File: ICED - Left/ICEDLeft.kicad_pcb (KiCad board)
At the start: 2 copper layers, 175.4 x 145 mm, 150 parts, among them P1 Conn_ARM_JTAG_SWD_10, P2 USBC, P3 CONN_17, P4 USB3_AFEMALE, P5 RGB Out, Q1 TC1264, U1 MK20DX256VLH7, U2 IS31FL3737-QFLS4-TR, X1 CRYSTAL

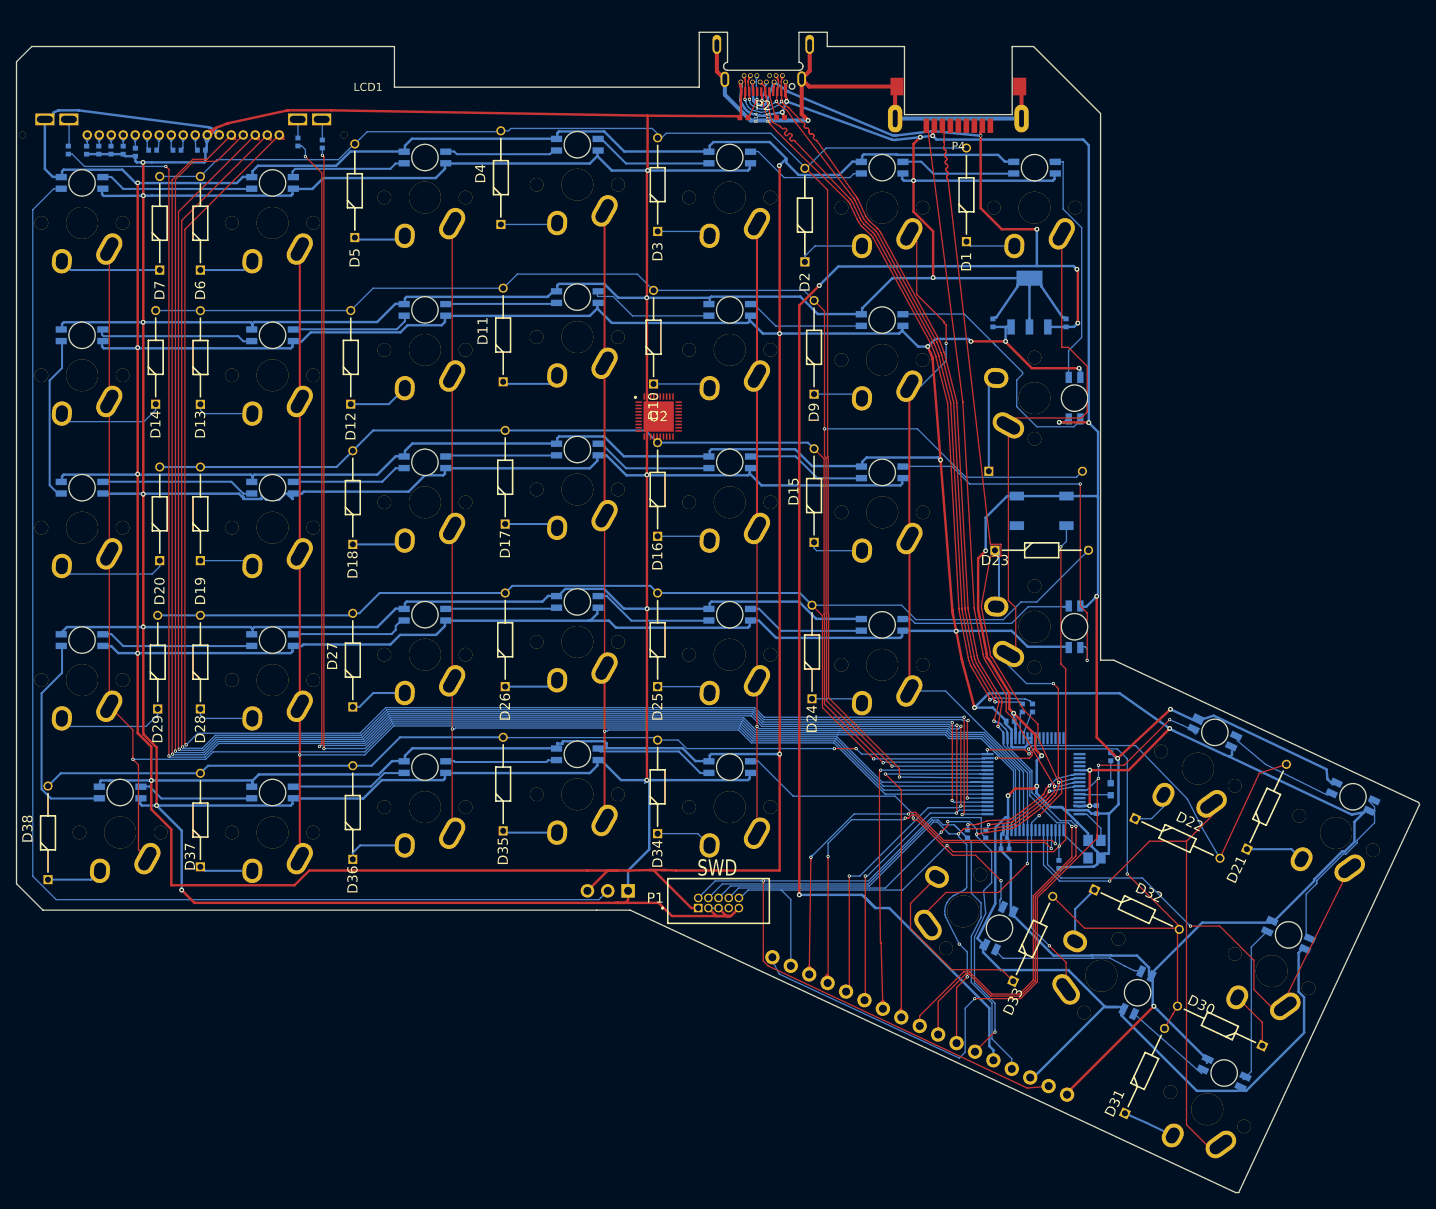
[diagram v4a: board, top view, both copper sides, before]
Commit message: Added support caps
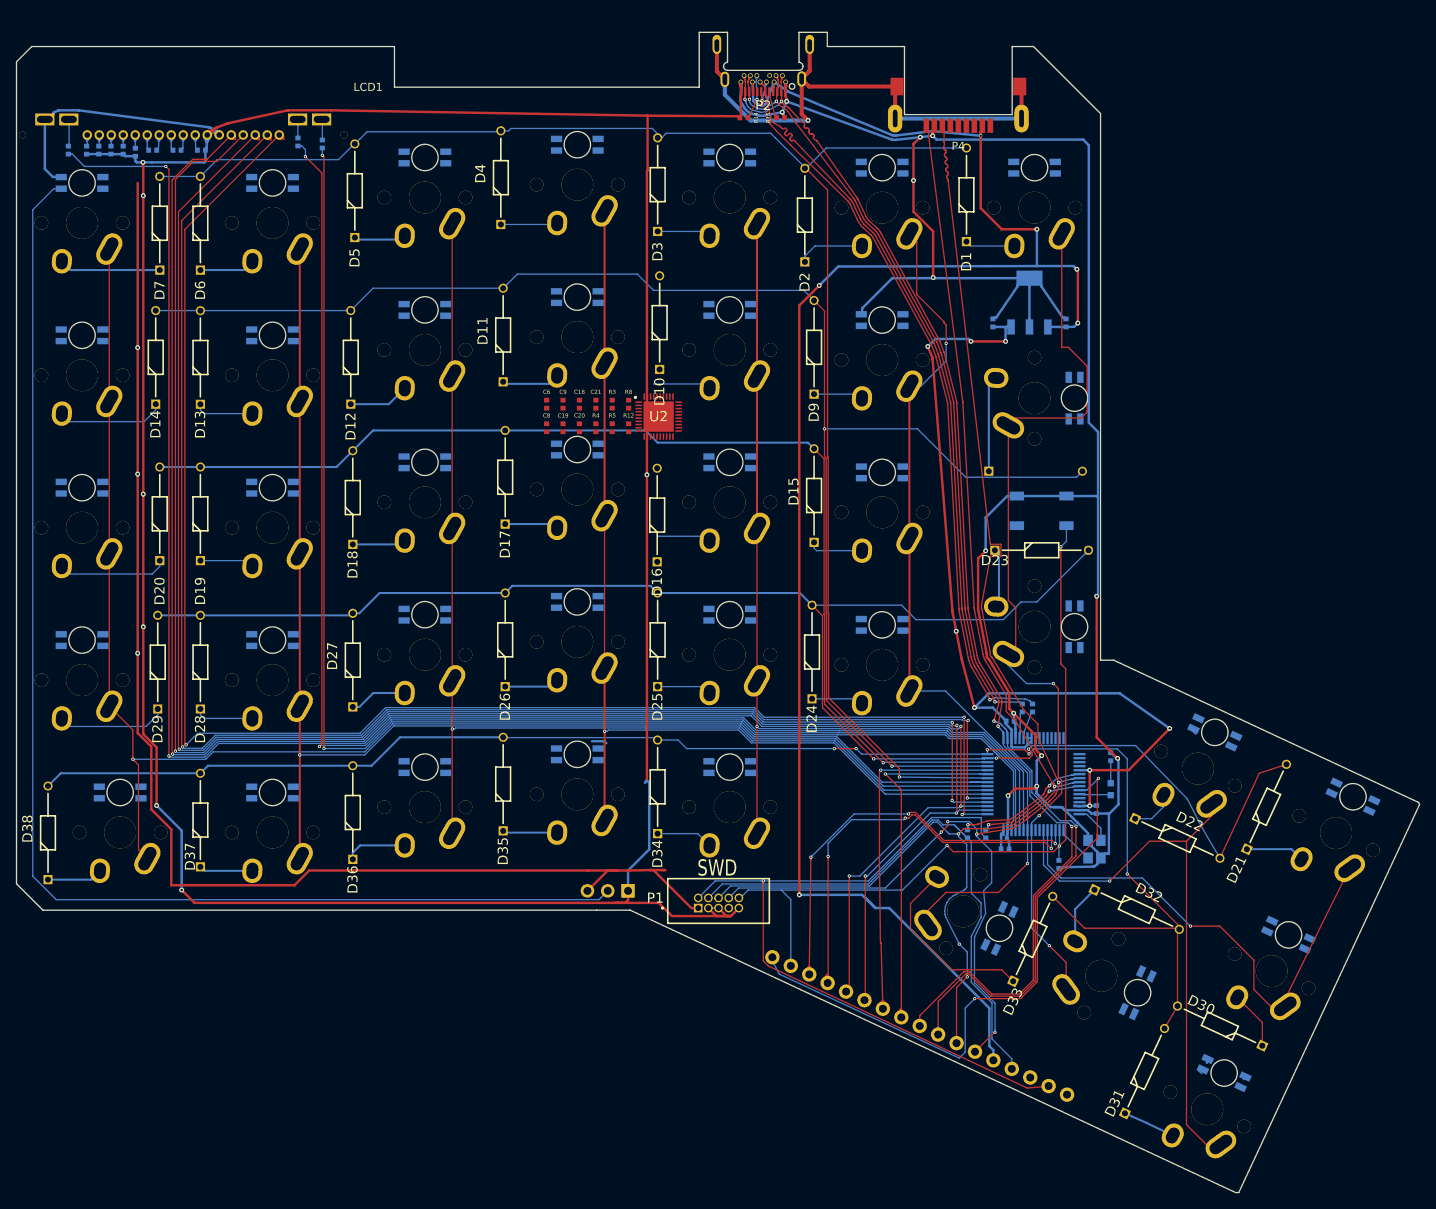
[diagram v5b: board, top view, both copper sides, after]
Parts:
- added C18: 0.1uF, prettylib:SMD-1005, F.Cu at (88.0, 72.3)
- added C19: 0.1uF, prettylib:SMD-1005, F.Cu at (86.0, 75.2)
- added C20: 0.1uF, prettylib:SMD-1005, F.Cu at (88.0, 75.2)
- added C21: 0.47uF, prettylib:SMD-1005, F.Cu at (90.1, 72.3)
- added C6: 0.47uF, prettylib:SMD-1005, F.Cu at (83.9, 72.3)
- added C8: 0.47uF, prettylib:SMD-1005, F.Cu at (83.9, 75.2)
- added C9: 0.47uF, prettylib:SMD-1005, F.Cu at (86.0, 72.3)
- added R12: 20k, prettylib:SMD-1005, F.Cu at (94.2, 75.2)
- added R3: 4.7, prettylib:SMD-1005, F.Cu at (92.1, 72.3)
- added R4: 100k, prettylib:SMD-1005, F.Cu at (90.1, 75.2)
- added R5: 4.7, prettylib:SMD-1005, F.Cu at (92.1, 75.2)
- added R8: 100k, prettylib:SMD-1005, F.Cu at (94.2, 72.3)
- moved D16 3.20 mm to (97.7, 92.0)
- moved D10 1.97 mm to (98.0, 67.9)
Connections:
- U1 pad 39: (no net) -> /mcu/SDB
- U1 pad 40: (no net) -> /Col7
- U1 pad 55: /Col7 -> (no net)
- U1 pad 56: /Col8 -> (no net)
- U2 pad 19: (no net) -> VDD
- U2 pad 26: (no net) -> VDD
- U2 pad 29: (no net) -> /mcu/ledmatrix_2/GND
- U2 pad 31: (no net) -> VDD
- U2 pad 34: (no net) -> /mcu/SDA0
- U2 pad 35: (no net) -> /mcu/SCL0
- U2 pad 36: (no net) -> /mcu/ledmatrix_2/GND
- U2 pad 38: (no net) -> /mcu/SDB
- U2 pad 39: (no net) -> /mcu/ledmatrix_2/IICRST
- U2 pad 4: (no net) -> /mcu/ledmatrix_2/GND
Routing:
- net VDD: track 1142.2 -> 320.8 mm, vias 19 -> 11
- net VSS: track 1298.4 -> 672.9 mm, vias 28 -> 20
- net /ledmatrix/RGBIN: track 92.8 -> 0.00 mm, vias 4 -> 0
- net /mcu/RGBIN: track 0.00 -> 76.1 mm, vias 0 -> 2
- net /mcu/ledmatrix_2/Green3: track 66.0 -> 0.00 mm
- net /mcu/ledmatrix_2/Row1A: track 49.1 -> 0.00 mm
- net /mcu/ledmatrix_2/Row3A: track 48.9 -> 0.00 mm
- net /mcu/ledmatrix_2/Row4B: track 48.1 -> 0.00 mm, vias 2 -> 0
- net /mcu/ledmatrix_2/Green1: track 47.4 -> 0.96 mm
- net /mcu/ledmatrix_2/Row5A: track 44.2 -> 0.00 mm
- net /mcu/ledmatrix_2/Row5B: track 41.5 -> 0.69 mm, vias 2 -> 0
- net Net-(LED8-Pad4): track 32.4 -> 0.00 mm
- net /mcu/ledmatrix_2/Row1B: track 30.3 -> 0.37 mm
- net /mcu/ledmatrix_2/Row2B: track 29.8 -> 0.00 mm
- net Net-(LED23-Pad4): track 22.6 -> 0.00 mm
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
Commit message: left 50% routed
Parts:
- moved R4 25.4 mm to (107.7, 93.5)
- moved R3 24.9 mm to (104.4, 94.0)
- moved R8 23.5 mm to (103.0, 94.1)
- moved R5 23.4 mm to (106.1, 94.0)
- moved C8 18.6 mm to (102.5, 74.2), turned to 180 degrees
- moved C19 17.9 mm to (103.8, 74.2), turned to 180 degrees
- moved C6 16.6 mm to (99.2, 78.9), turned to 180 degrees
- moved C9 15.5 mm to (101.1, 69.0)
- moved C18 13.9 mm to (100.3, 78.9), turned to 180 degrees
- moved C20 13.4 mm to (99.9, 69.0)
- moved C21 9.05 mm to (98.5, 69.0)
- moved R12 8.67 mm to (102.3, 72.3), turned to 90 degrees
- moved D10 1.17 mm to (96.9, 67.7)
- moved D26 0.90 mm to (78.6, 106.7)
- moved D36 0.63 mm to (59.2, 128.8)
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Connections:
- R12 pad 1: VSS -> /mcu/ledmatrix_2/RSET
- R12 pad 2: (no net) -> VSS
- U2 pad 30: (no net) -> /mcu/ledmatrix_2/RSET
- U2 pad 32: (no net) -> VDD
- U2 pad 6: /mcu/ledmatrix_2/Blue2 -> /mcu/ledmatrix_2/Green2
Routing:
- net /mcu/ledmatrix_2/Blue1: track 0.00 -> 196.9 mm, vias 0 -> 7
- net /mcu/ledmatrix_2/Green1: track 0.96 -> 193.6 mm, vias 0 -> 7
- net /mcu/ledmatrix_2/Red1: track 0.00 -> 185.1 mm, vias 0 -> 7
- net VSS: track 672.9 -> 488.1 mm, vias 20 -> 13
- net /mcu/ledmatrix_2/Blue2: track 0.00 -> 176.4 mm, vias 0 -> 7
- net /mcu/ledmatrix_2/Green2: track 0.00 -> 166.5 mm, vias 0 -> 7
- net (no net): track 162.0 -> 0.26 mm
- net /mcu/ledmatrix_2/Red2: track 0.00 -> 143.2 mm, vias 0 -> 7
- net /mcu/ledmatrix_2/Blue3: track 0.00 -> 142.1 mm, vias 0 -> 7
- net VDD: track 320.8 -> 181.5 mm, vias 11 -> 8
- net /mcu/ledmatrix_2/Green3: track 0.00 -> 138.3 mm, vias 0 -> 7
- net /mcu/ledmatrix_2/Blue4: track 1.91 -> 129.9 mm, vias 0 -> 7
- net /mcu/ledmatrix_2/Red3: track 0.00 -> 126.8 mm, vias 0 -> 7
- net /mcu/ledmatrix_2/Row5A: track 0.00 -> 122.5 mm, vias 0 -> 1
- net /mcu/ledmatrix_2/Green4: track 0.44 -> 122.1 mm, vias 0 -> 8
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
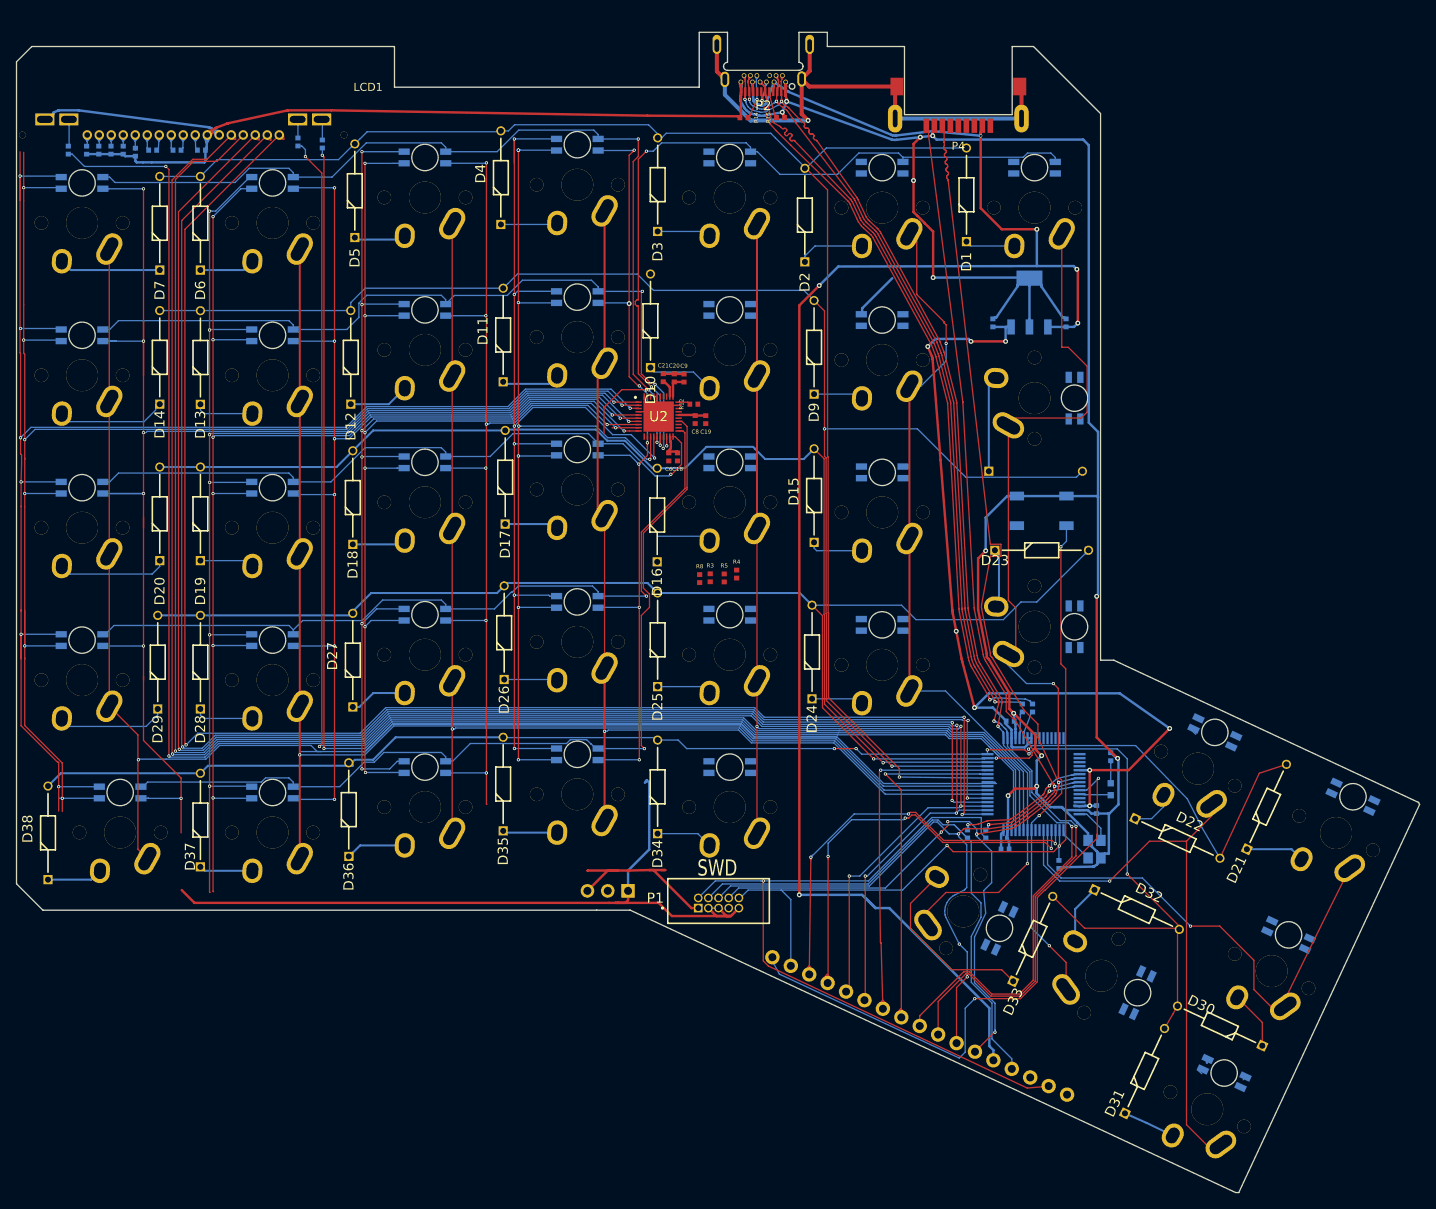
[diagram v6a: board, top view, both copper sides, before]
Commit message: Routed new USB ports
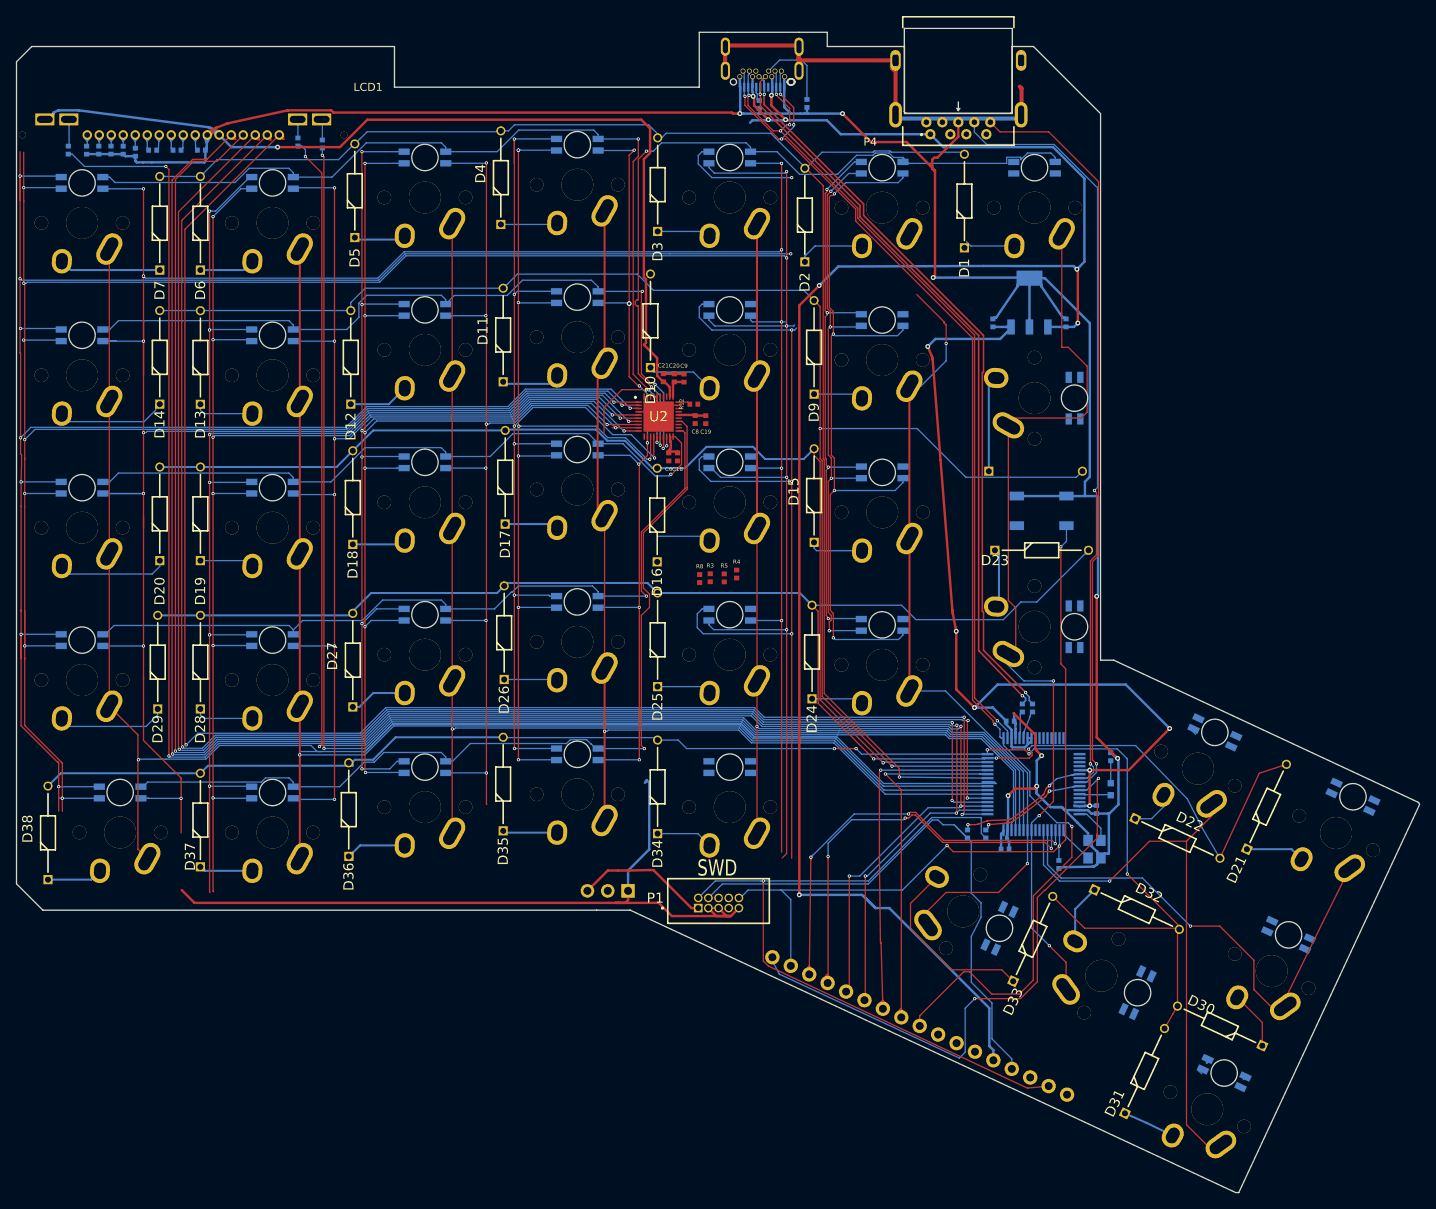
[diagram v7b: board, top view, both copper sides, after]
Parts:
- P2: value USBC -> DX07S024XJ1R1100; footprint prettylib:USB_C_MIDMOUNT_TH_IMPCUT -> prettylib:JAE_DX07S024XJ1R1100; moved to B.Cu
- P4: value USB3_AFEMALE -> 692121130100; footprint prettylib:USB3_AFEMALE_MOD -> prettylib:692121130100
- R14, R15: moved to B.Cu
- moved P4 4.32 mm to (135.4, 31.9)
- moved P2 3.77 mm to (107.3, 32.0), turned to 0 degrees
- moved R15 3.75 mm to (116.5, 34.7), turned to 180 degrees
- moved R14 2.52 mm to (110.5, 34.8), turned to 180 degrees
- moved D1 0.82 mm to (136.1, 52.7)
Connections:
- P4 pad 4: VSS -> (no net)
- P4 pad 7: (no net) -> VSS
- R1 pad 1: /mcu/USB_DP -> /mcu/D+
- R14 pad 1: Net-(P2-Pad17) -> Net-(P2-PadA5)
- R15 pad 1: Net-(P2-Pad5) -> Net-(P2-PadB5)
- R2 pad 1: /mcu/USB_DM -> /mcu/D-
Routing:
- net /mcu/ledmatrix_2/Green1: track 193.6 -> 419.5 mm, vias 7 -> 13
- net /mcu/ledmatrix_2/Blue1: track 196.9 -> 422.0 mm, vias 7 -> 13
- net /mcu/ledmatrix_2/Red1: track 185.1 -> 369.4 mm, vias 7 -> 14
- net /mcu/USB_DM: track 96.0 -> 0.00 mm, vias 2 -> 0
- net /mcu/ledmatrix_2/Red2: track 143.2 -> 238.6 mm, vias 7 -> 11
- net /mcu/D+: track 0.00 -> 93.9 mm, vias 0 -> 2
- net /mcu/USB_DP: track 93.3 -> 0.00 mm, vias 1 -> 0
- net /mcu/D-: track 0.00 -> 93.2 mm, vias 0 -> 2
- net VDD: track 181.5 -> 265.9 mm, vias 8 -> 7
- net /mcu/RX0: track 174.4 -> 95.7 mm, vias 5 -> 2
- net /mcu/TX0: track 169.7 -> 93.6 mm, vias 4 -> 1
- net /mcu/ledmatrix_2/Green2: track 166.5 -> 239.0 mm, vias 7 -> 11
- net /mcu/ledmatrix_2/Blue2: track 176.4 -> 243.0 mm, vias 7 -> 11
- net VSS: track 488.1 -> 424.4 mm, vias 13 -> 8
- net /mcu/RX1: track 160.3 -> 106.5 mm, vias 4 -> 5
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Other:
- outline, holes or cut-outs redrawn
